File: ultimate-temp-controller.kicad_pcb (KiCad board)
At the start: 2 copper layers, 80 x 100 mm, 68 parts, among them CON1 SD_Card, IC1 ATMEGA328-A, P1 ISP, P10 RS485, P2 BUTTONS, P3 OPEN_DRAIN, P4 POWER, P5 I2C1, P6 I2C2, P7 CONN_01X05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

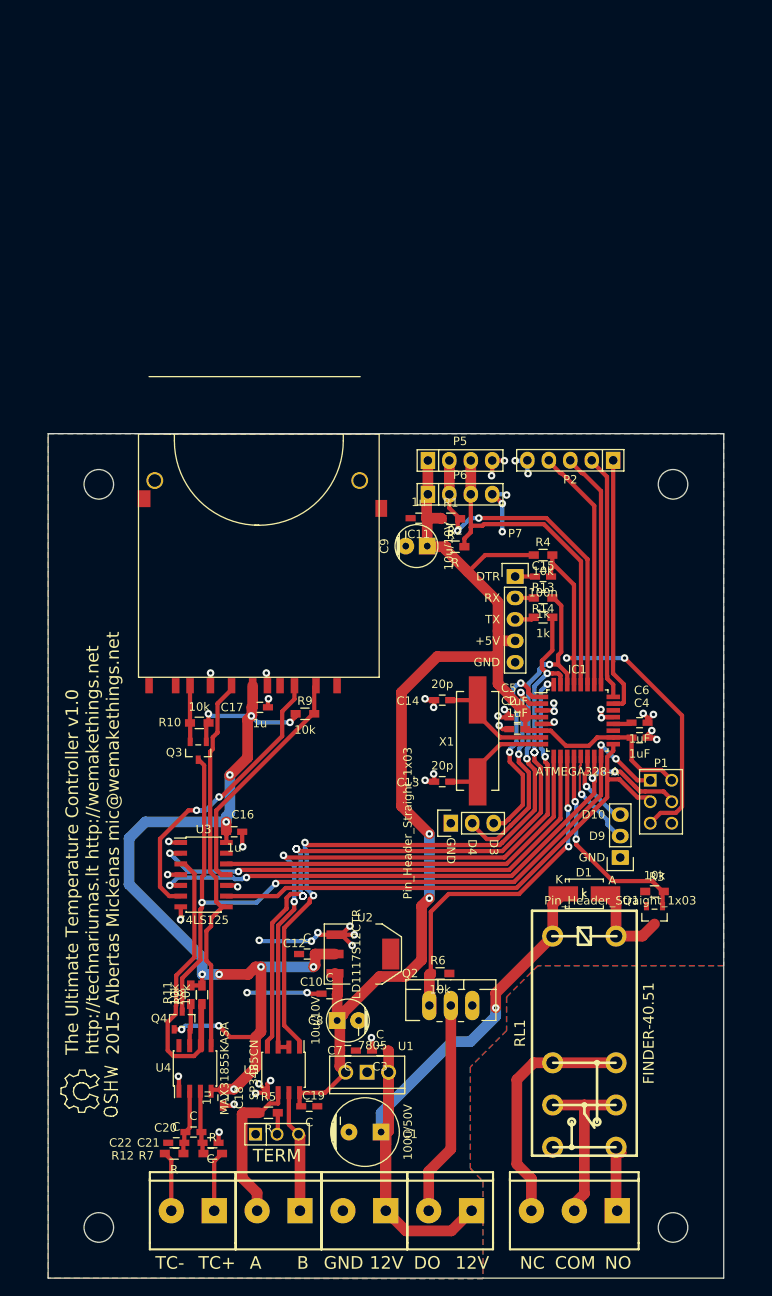
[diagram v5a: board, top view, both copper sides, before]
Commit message: Use 4050 as a level shifter
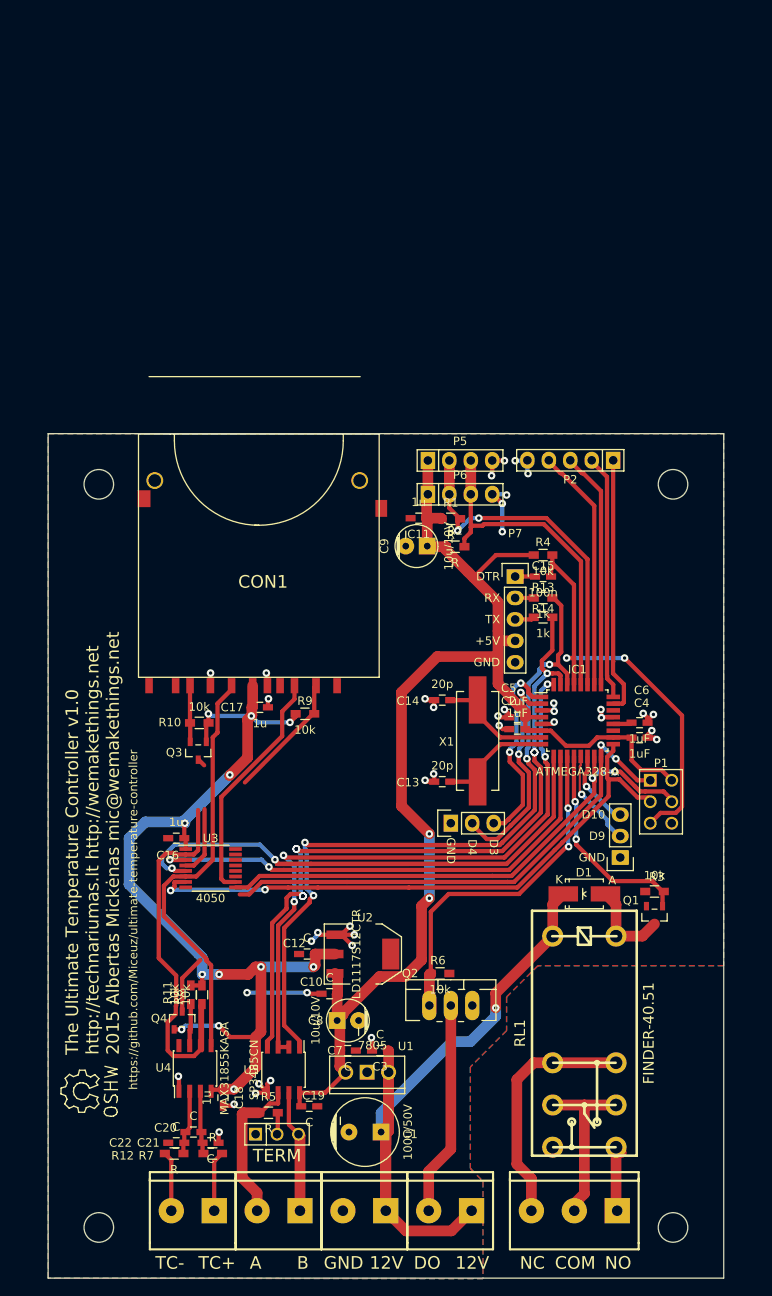
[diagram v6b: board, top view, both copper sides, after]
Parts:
- CON1: footprint SD-CARD-PROCON-19608 -> w_conn_misc:SD-CARD-PROCON-19608
- U3: value 74LS125 -> 4050; footprint Housings_SOIC:SOIC-14_3.9x8.7mm_Pitch1.27mm -> Housings_SSOP:TSSOP-16_4.4x5mm_Pitch0.65mm
- moved C16 6.90 mm to (106.2, 136.9), turned to 180 degrees
- moved U3 1.13 mm to (110.2, 140.5)
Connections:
- U3 pad 1: GND -> +3V3
- U3 pad 10: GND -> /controller/MOSI_3V3
- U3 pad 11: /controller/CS_SD_3V3 -> GND
- U3 pad 12: /controller/CS_SD -> Net-(U3-Pad12)
- U3 pad 13: GND -> (no net)
- U3 pad 14: +3V3 -> GND
- U3 pad 2: /controller/CS_TC -> /controller/CS_TC_3V3
- U3 pad 3: /controller/CS_TC_3V3 -> /controller/CS_TC
- U3 pad 4: GND -> /controller/CS_SD_3V3
- U3 pad 5: /controller/MOSI -> /controller/CS_SD
- U3 pad 6: /controller/MOSI_3V3 -> /controller/CLK_3V3
- U3 pad 7: GND -> /controller/CLK
- U3 pad 8: /controller/CLK_3V3 -> GND
- U3 pad 9: /controller/CLK -> /controller/MOSI
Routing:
- net /controller/CS_SD: track 48.2 -> 88.7 mm, vias 0 -> 2
- net /controller/MISO: track 97.8 -> 69.7 mm, vias 4 -> 2
- net GND: track 80.6 -> 66.2 mm, vias 46 -> 40
- net /controller/CS_TC_3V3: track 39.7 -> 49.2 mm
- net /controller/MOSI: track 72.7 -> 63.3 mm, vias 4 -> 2
- net /controller/CLK: track 63.0 -> 71.7 mm, vias 0 -> 2
- net /controller/MOSI_3V3: track 35.7 -> 28.3 mm, vias 2 -> 0
- net /controller/CS_SD_3V3: track 28.7 -> 23.2 mm
- net /controller/CLK_3V3: track 46.3 -> 49.9 mm
- net +3V3: track 118.6 -> 117.1 mm
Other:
- net class Default: clearance 0.2032 -> 0.1
- rule trace_clearance: 0.2032 -> 0.1
- board text added: "https://github.com/Miceuz/ultimate-temperature-controller"

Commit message: Turn 4050 180 degrees, enjoy better routing, move spare pins near ISP header
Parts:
- moved C16 9.20 mm to (112.0, 144.0)
- moved Pin_Header_Straight_1x03 8.77 mm to (167.4, 137.7), turned to 270 degrees
- moved U3 0.25 mm to (110.2, 140.2), turned to 180 degrees
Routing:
- net /controller/MISO: track 69.7 -> 104.9 mm, vias 2 -> 4
- net GND: track 66.2 -> 83.2 mm, vias 40 -> 46
- net +3V3: track 117.1 -> 133.8 mm, vias 12 -> 14
- net /controller/CS_SD: track 88.7 -> 74.9 mm, vias 2 -> 0
- net Net-(IC1-Pad13): track 11.6 -> 24.9 mm, vias 1 -> 2
- net /controller/CS_TC_3V3: track 49.2 -> 38.0 mm
- net /controller/CS_TC: track 58.5 -> 48.6 mm, vias 2 -> 0
- net /controller/MOSI: track 63.3 -> 71.8 mm, vias 2 -> 4
- net Net-(IC1-Pad14): track 9.76 -> 17.1 mm, vias 1 -> 2
- net /controller/CLK: track 71.7 -> 65.1 mm
- net /controller/CS_SD_3V3: track 23.2 -> 29.2 mm, vias 0 -> 2
- net /controller/CLK_3V3: track 49.9 -> 46.0 mm
- net +5V: track 157.2 -> 159.7 mm
- net (no net): track 0.00 -> 1.91 mm, vias 0 -> 1
- net /controller/SDA: track 41.8 -> 42.7 mm
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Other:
- net class Default: clearance 0.1 -> 0.127
- net class mosi3v3 added: clearance 0.127, trace_width 0.45, via_dia 0.9, via_drill 0.4
- rule trace_clearance: 0.1 -> 0.127

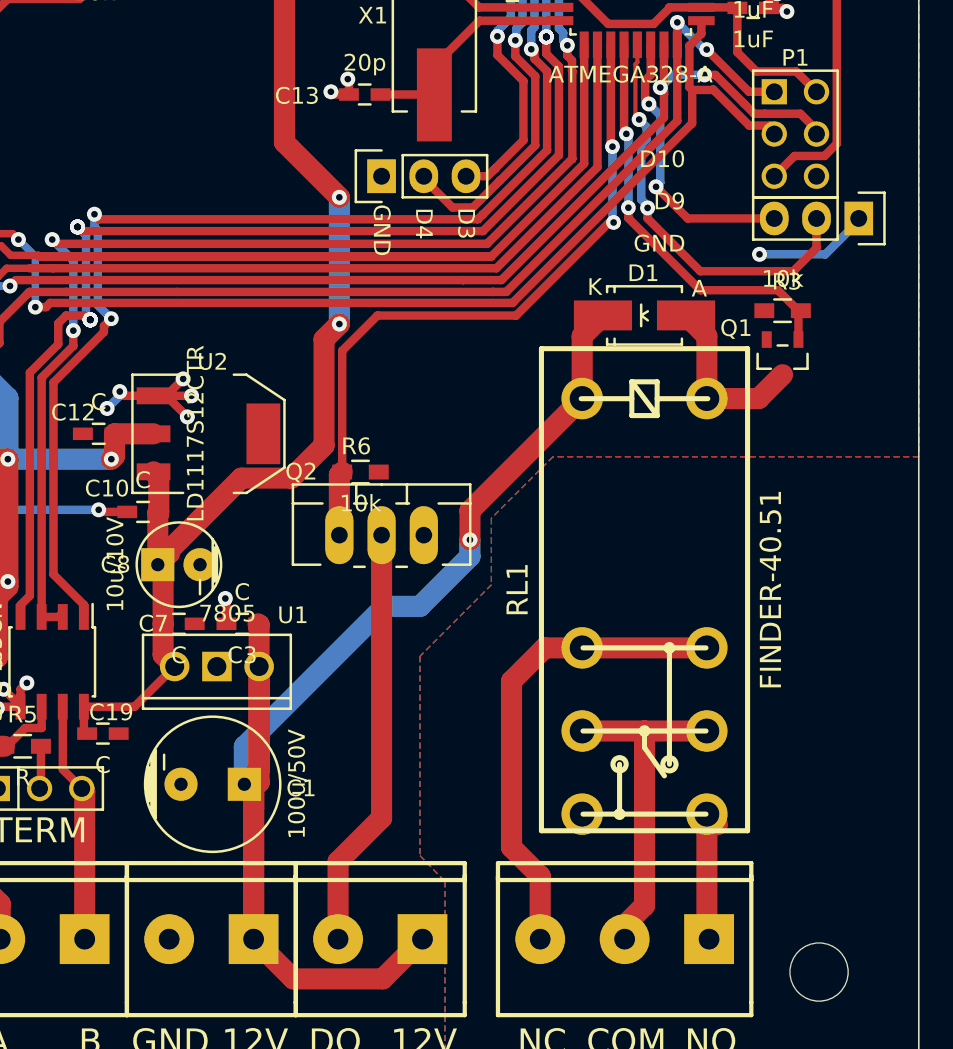
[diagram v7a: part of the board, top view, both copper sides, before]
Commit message: Add mounting hole for expansion header, add a hole near screw terminals for more support
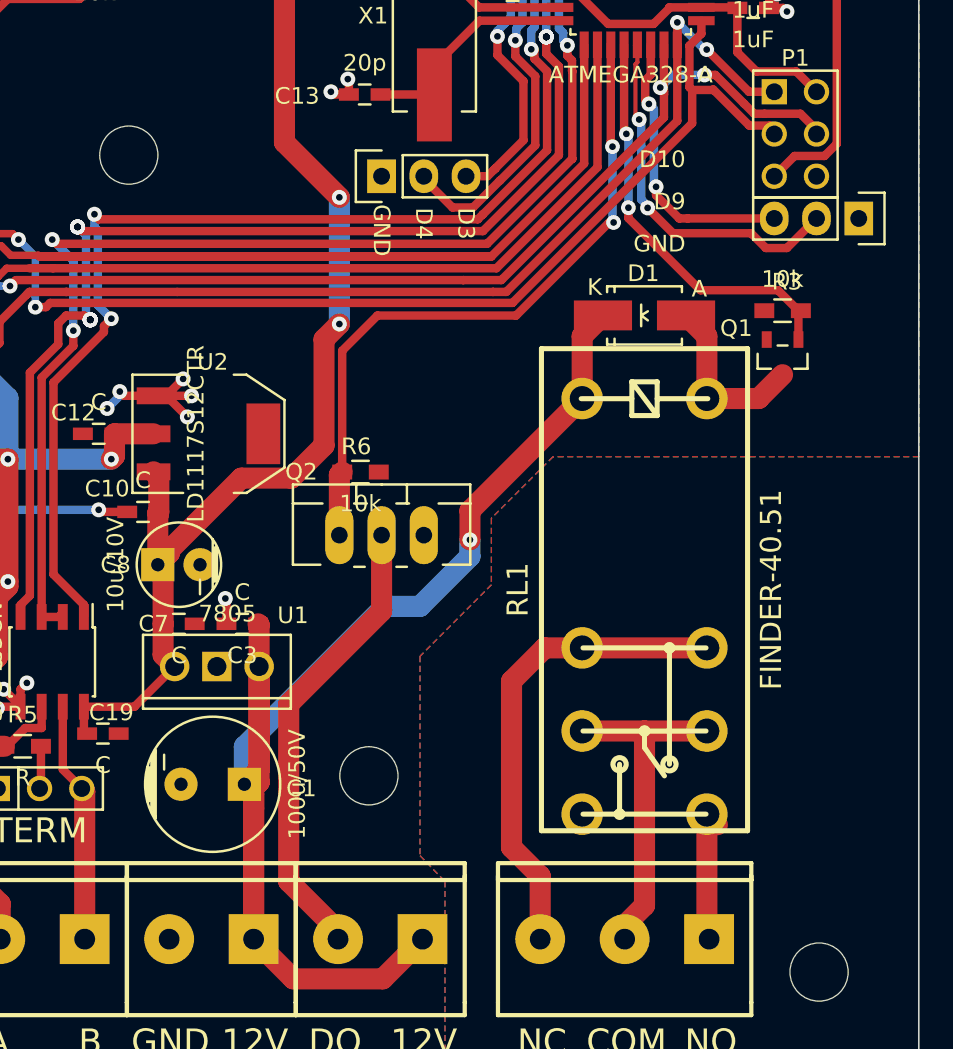
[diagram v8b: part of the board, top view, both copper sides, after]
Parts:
- added MountingHole_3-5mm: VAL**, Mounting_Holes:MountingHole_3-5mm, F.Cu at (137.9, 171.2)
- added MountingHole_3-5mm: VAL**, Mounting_Holes:MountingHole_3-5mm, F.Cu at (123.5, 133.9)
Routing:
- net GND: track 83.2 -> 76.4 mm, vias 46 -> 45
- net Net-(IC1-Pad13): track 24.9 -> 22.1 mm
- net /controller/DRAIN: track 25.4 -> 27.8 mm
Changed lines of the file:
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@@
     (area 90.949999 88.949999 171.050001 189.050001)
     (thickness 1.6)
-    (drawings 46)
-    (tracks 856)
+    (drawings 52)
+    (tracks 857)
     (zones 0)
-    (modules 68)
+    (modules 70)
     (nets 57)
   )
@@
   )
   (setup
-    (last_trace_width 0.508)
+    (last_trace_width 1.27)
     (user_trace_width 0.45)
     (user_trace_width 0.508)
@@
     (add_net /controller/MOSI_3V3)
   )
+  (module Mounting_Holes:MountingHole_3-5mm (layer F.Cu)
+    (at 137.922 171.196)
+    (descr "Mounting hole, Befestigungsbohrung, 3,5mm, No Annular, Kein Restring,")
+    (tags "Mounting hole, Befestigungsbohrung, 3,5mm, No Annular, Kein Restring,")
+    (fp_text reference MountingHole_3-5mm (at 0 -4.50088) (layer F.SilkS) hide
+      (effects (font (size 1 1) (thickness 0.15)))
+    )
+    (fp_text value VAL** (at 0 5.00126) (layer F.SilkS) hide
+      (effects (font (size 1 1) (thickness 0.15)))
+    )
+    (fp_circle (center 0 0) (end 3.50012 0) (layer Cmts.User) (width 0.381))
+    (pad 1 thru_hole circle (at 0 0) (size 3.50012 3.50012) (drill 3.50012) (layers))
+  )
+  (module Mounting_Holes:MountingHole_3-5mm locked (layer F.Cu)
+    (at 123.48 133.858)
+    (descr "Mounting hole, Befestigungsbohrung, 3,5mm, No Annular, Kein Restring,")
+    (tags "Mounting hole, Befestigungsbohrung, 3,5mm, No Annular, Kein Restring,")
+    (fp_text reference MountingHole_3-5mm (at 0 -4.50088) (layer F.SilkS) hide
+      (effects (font (size 1 1) (thickness 0.15)))
+    )
+    (fp_text value VAL** (at 0 5.00126) (layer F.SilkS) hide
+      (effects (font (size 1 1) (thickness 0.15)))
+    )
+    (fp_circle (center 0 0) (end 3.50012 0) (layer Cmts.User) (width 0.381))
+    (pad 1 thru_hole circle (at 0 0) (size 3.50012 3.50012) (drill 3.50012) (layers))
+  )
   (module Housings_SSOP:TSSOP-16_4.4x5mm_Pitch0.65mm (layer F.Cu)
     (at 110.236 140.208 180)
@@
     )
   )
+  (gr_line (start 170.942 142.24) (end 170.18 142.24) (angle 90) (layer Cmts.User) (width 0.2))
+  (gr_line (start 170.942 124.46) (end 170.942 142.24) (angle 90) (layer Cmts.User) (width 0.2))
+  (gr_line (start 169.926 124.46) (end 170.942 124.46) (angle 90) (layer Cmts.User) (width 0.2))
+  (gr_line (start 116.84 142.24) (end 170.18 142.24) (angle 90) (layer Cmts.User) (width 0.2))
+  (gr_line (start 116.84 124.46) (end 116.84 142.24) (angle 90) (layer Cmts.User) (width 0.2))
+  (gr_line (start 170.18 124.46) (end 116.84 124.46) (angle 90) (layer Cmts.User) (width 0.2))
   (gr_text https://github.com/Miceuz/ultimate-temperature-controller (at 101.092 146.558 90) (layer F.SilkS)
     (effects (font (size 1 1) (thickness 0.15)))
@@
   (segment (start 144 157) (end 144 155.25) (width 1.27) (layer F.Cu) (net 1))
   (segment (start 167.386 137.668) (end 167.386 137.8204) (width 0.508) (layer B.Cu) (net 2))
-  (segment (start 167.386 137.8204) (end 165.3794 139.827) (width 0.508) (layer B.Cu) (net 2))
-  (segment (start 165.3794 139.827) (end 161.417 139.827) (width 0.508) (layer B.Cu) (net 2))
-  (via (at 161.417 139.827) (size 0.9) (drill 0.4) (layers F.Cu B.Cu) (net 2))
   (segment (start 111.125 145.288) (end 111.125 145.7198) (width 0.254) (layer B.Cu) (net 2))
   (segment (start 114.046 148.6408) (end 114.0206 148.6408) (width 0.254) (layer F.Cu) (net 2))
@@
   (segment (start 150.556 105.035) (end 150.706 104.885) (width 0.508) (layer F.Cu) (net 39))
   (segment (start 150.556 105.918) (end 150.556 105.035) (width 0.508) (layer F.Cu) (net 39))
-  (segment (start 138.684 156.718) (end 138.684 173.736) (width 1.27) (layer F.Cu) (net 40) (status 10))
-  (segment (start 136.065 176.355) (end 136.065 181.02) (width 1.27) (layer F.Cu) (net 40) (status 20))
-  (segment (start 138.684 173.736) (end 136.065 176.355) (width 1.27) (layer F.Cu) (net 40))
+  (segment (start 136.065 181.02) (end 136.065 180.515) (width 1.27) (layer F.Cu) (net 40))
+  (segment (start 136.065 180.515) (end 133.096 177.546) (width 1.27) (layer F.Cu) (net 40))
+  (segment (start 133.096 166.878) (end 138.684 161.29) (width 1.27) (layer F.Cu) (net 40))
+  (segment (start 133.096 177.546) (end 133.096 166.878) (width 1.27) (layer F.Cu) (net 40))
+  (segment (start 138.684 156.718) (end 138.684 161.29) (width 1.27) (layer F.Cu) (net 40) (status 10))
   (segment (start 158.25 173.5) (end 158.25 180.885) (width 1.27) (layer F.Cu) (net 41) (status 30))
   (segment (start 158.25 180.885) (end 158.385 181.02) (width 1.27) (layer F.Cu) (net 41) (status 30))
@@
   (segment (start 107.018 174.244) (end 107.018 173.078) (width 0.508) (layer F.Cu) (net 49) (status 30))
   (segment (start 107.018 173.078) (end 107.122 172.974) (width 0.508) (layer F.Cu) (net 49) (status 30))
-  (segment (start 155.194 135.763) (end 157.099 137.668) (width 0.508) (layer F.Cu) (net 50))
-  (segment (start 157.099 137.668) (end 162.306 137.668) (width 0.508) (layer F.Cu) (net 50))
-  (segment (start 155.448 131.464786) (end 155.448 135.509) (width 0.508) (layer B.Cu) (net 50))
-  (segment (start 155.448 135.509) (end 155.194 135.763) (width 0.508) (layer B.Cu) (net 50))
+  (segment (start 155.194 135.763) (end 155.194 136.271) (width 0.508) (layer F.Cu) (net 50))
+  (segment (start 156.591 137.668) (end 157.099 137.668) (width 0.508) (layer F.Cu) (net 50))
+  (segment (start 155.194 136.271) (end 156.591 137.668) (width 0.508) (layer F.Cu) (net 50))
+  (segment (start 154.763948 130.780734) (end 155.067 131.083786) (width 0.508) (layer B.Cu) (net 50))
+  (segment (start 155.067 135.636) (end 155.194 135.763) (width 0.508) (layer B.Cu) (net 50))
+  (segment (start 155.067 132.08) (end 155.067 135.636) (width 0.508) (layer B.Cu) (net 50))
+  (segment (start 155.067 131.083786) (end 155.067 132.08) (width 0.508) (layer B.Cu) (net 50))
   (via (at 155.194 135.763) (size 0.9) (drill 0.4) (layers F.Cu B.Cu) (net 50))
-  (segment (start 154.763948 130.780734) (end 155.448 131.464786) (width 0.508) (layer B.Cu) (net 50))
+  (segment (start 157.099 137.668) (end 162.306 137.668) (width 0.508) (layer F.Cu) (net 50))
   (segment (start 154.540799 130.557585) (end 154.763948 130.780734) (width 0.508) (layer F.Cu) (net 50))
   (via (at 154.763948 130.780734) (size 0.9) (drill 0.4) (layers F.Cu B.Cu) (net 50))
@@
   (segment (start 154.871158 129.028184) (end 154.540799 129.358543) (width 0.508) (layer F.Cu) (net 50))
   (segment (start 154.871158 127.221318) (end 154.871158 129.028184) (width 0.508) (layer F.Cu) (net 50))
-  (segment (start 163.449 140.843) (end 164.846 139.446) (width 0.508) (layer F.Cu) (net 51))
-  (segment (start 164.846 139.446) (end 164.846 137.668) (width 0.508) (layer F.Cu) (net 51))
-  (segment (start 157.859604 140.843) (end 163.449 140.843) (width 0.508) (layer F.Cu) (net 51))
-  (segment (start 154.686 137.033) (end 154.686 137.669396) (width 0.508) (layer F.Cu) (net 51))
-  (segment (start 154.686 137.669396) (end 157.859604 140.843) (width 0.508) (layer F.Cu) (net 51))
+  (segment (start 154.686 137.033) (end 156.21 138.557) (width 0.508) (layer F.Cu) (net 51))
+  (segment (start 160.909 138.557) (end 161.798 139.446) (width 0.508) (layer F.Cu) (net 51))
+  (segment (start 156.21 138.557) (end 160.909 138.557) (width 0.508) (layer F.Cu) (net 51))
+  (segment (start 163.068 139.446) (end 164.846 137.668) (width 0.508) (layer F.Cu) (net 51))
+  (segment (start 161.798 139.446) (end 163.068 139.446) (width 0.508) (layer F.Cu) (net 51))
+  (segment (start 154.305 133.35) (end 154.305 131.842327) (width 0.508) (layer B.Cu) (net 51))
+  (segment (start 154.305 131.842327) (end 154.178365 131.715692) (width 0.508) (layer B.Cu) (net 51))
   (segment (start 154.305 136.525) (end 154.686 136.906) (width 0.508) (layer B.Cu) (net 51))
   (segment (start 154.686 136.906) (end 154.686 137.033) (width 0.508) (layer B.Cu) (net 51))
   (via (at 154.686 137.033) (size 0.9) (layers F.Cu B.Cu) (net 51))
-  (segment (start 154.305 133.223) (end 154.305 136.525) (width 0.508) (layer B.Cu) (net 51))
-  (segment (start 154.628364 132.899636) (end 154.305 133.223) (width 0.508) (layer B.Cu) (net 51))
-  (segment (start 154.178365 131.715692) (end 154.628364 132.165691) (width 0.508) (layer B.Cu) (net 51))
-  (segment (start 154.628364 132.165691) (end 154.628364 132.899636) (width 0.508) (layer B.Cu) (net 51))
+  (segment (start 154.305 133.35) (end 154.305 136.525) (width 0.508) (layer B.Cu) (net 51))
   (segment (start 154.054159 127.238317) (end 154.071158 127.221318) (width 0.508) (layer F.Cu) (net 51) (status 30))
   (via (at 154.178365 131.715692) (size 0.9) (layers F.Cu B.Cu) (net 51))
